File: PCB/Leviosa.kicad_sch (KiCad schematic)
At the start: 74 parts, among them J1 Barrel_Jack, J2 Conn_01x05_Socket, J3 2.54mm 1x03 Spare, Q1 NCE0110K, U1 STM32G030F6Px, U10 LM321, U2 TPS1H200AQDGNRQ1, U3 INA199A1DCKR, U4 L78L10_SOT89, U5 AZ1117CH2-3.3, U6 SS495A, U8 LM393, U9 MX27517

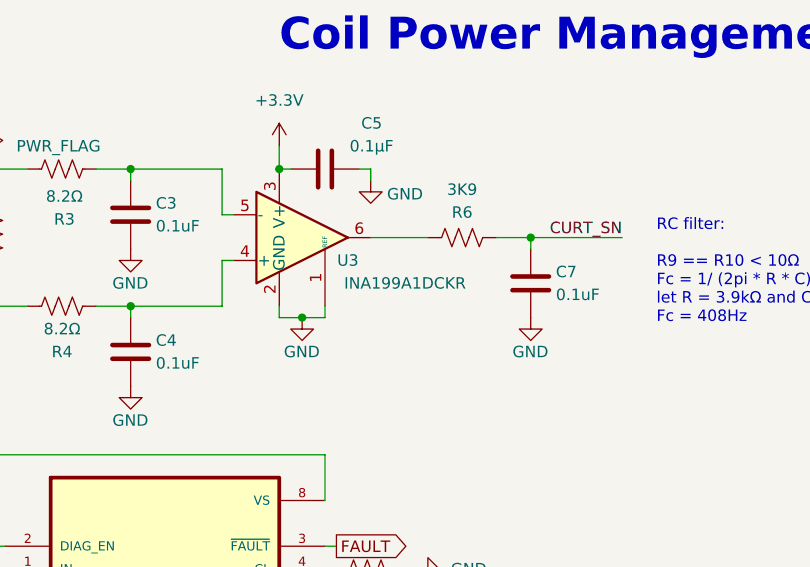
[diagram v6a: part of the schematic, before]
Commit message: Update current sense to 200V/V from 50V/V
Also updated footprint to hand solder version
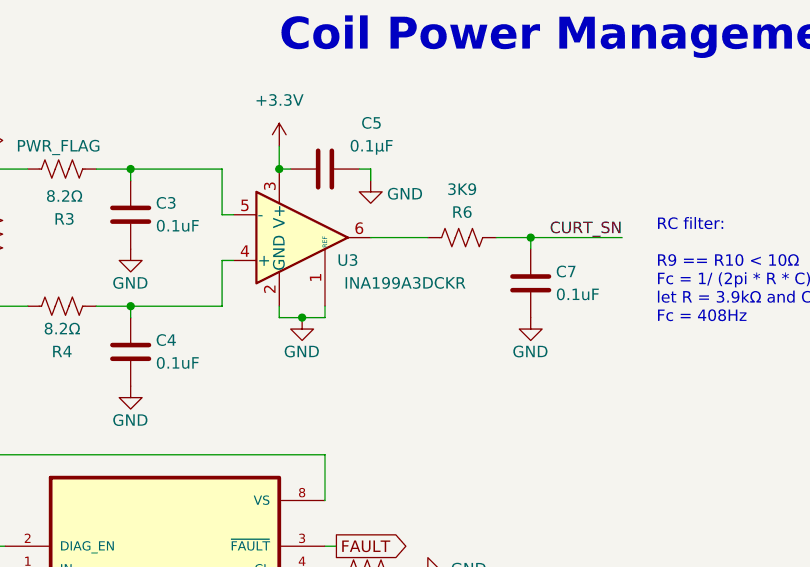
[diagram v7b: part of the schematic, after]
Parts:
- U3: value INA199A1DCKR -> INA199A3DCKR; footprint Package_TO_SOT_SMD:SOT-363_SC-70-6 -> Package_TO_SOT_SMD:SOT-363_SC-70-6_Handsoldering; Supplier https://www.lcsc.com/product-detail/C59135.html?s_z=n_INA199 -> https://www.lcsc.com/product-detail/C132098.html?s_z=n_INA1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
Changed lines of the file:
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@@
 			)
 		)
-		(property "Value" "INA199A1DCKR"
+		(property "Value" "INA199A3DCKR"
 			(at 100.33 49.53 0)
 			(effects
@@
 			)
 		)
-		(property "Footprint" "Package_TO_SOT_SMD:SOT-363_SC-70-6"
+		(property "Footprint" "Package_TO_SOT_SMD:SOT-363_SC-70-6_Handsoldering"
 			(at 90.17 43.18 0)
 			(effects
@@
 			)
 		)
-		(property "Supplier" "https://www.lcsc.com/product-detail/C59135.html?s_z=n_INA199"
+		(property "Supplier" "https://www.lcsc.com/product-detail/C132098.html?s_z=n_INA199&spm=wm.ssy.bg.3.xh&lcsc_vid=FgBdVFcAFQddBlFSEgVbXlBXRVlWBlZWRABaUgJXFgAxVlNRQ1RWVVVRQ1leVzsOAxUeFF5JWBYZEEoKFBINSQcJGk4dAgUUFAk%3D"
 			(at 88.9 44.45 0)
 			(effects

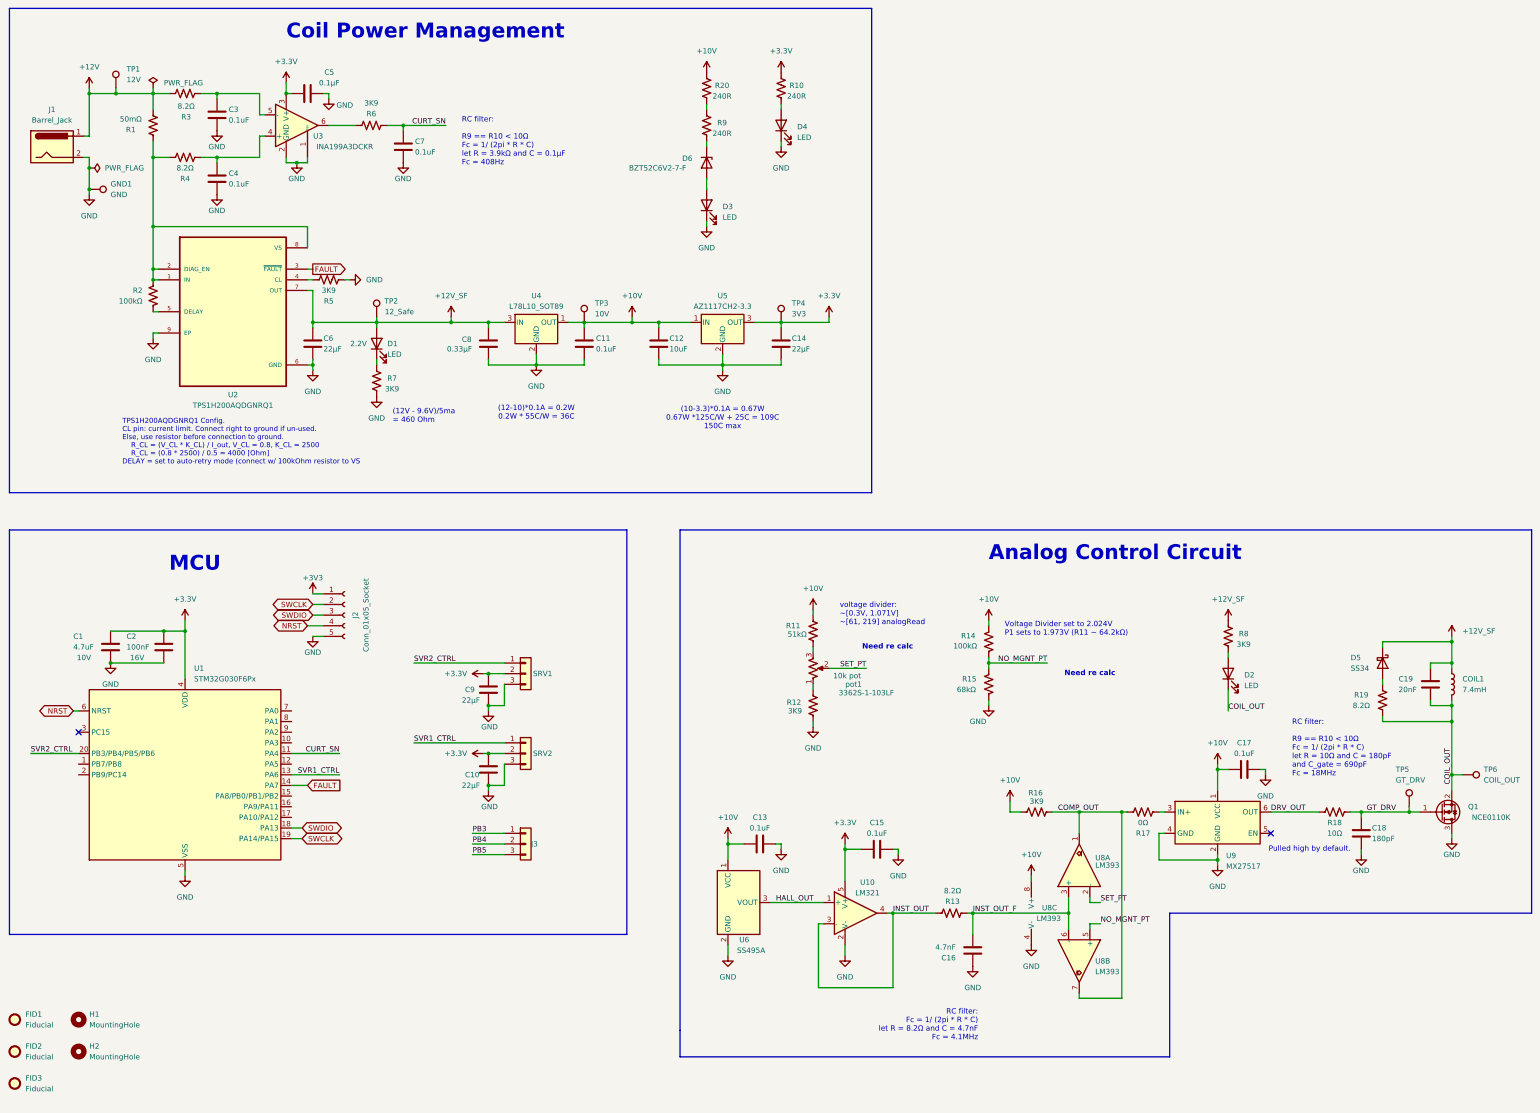
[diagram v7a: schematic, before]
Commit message: Changed LM321 to 10V
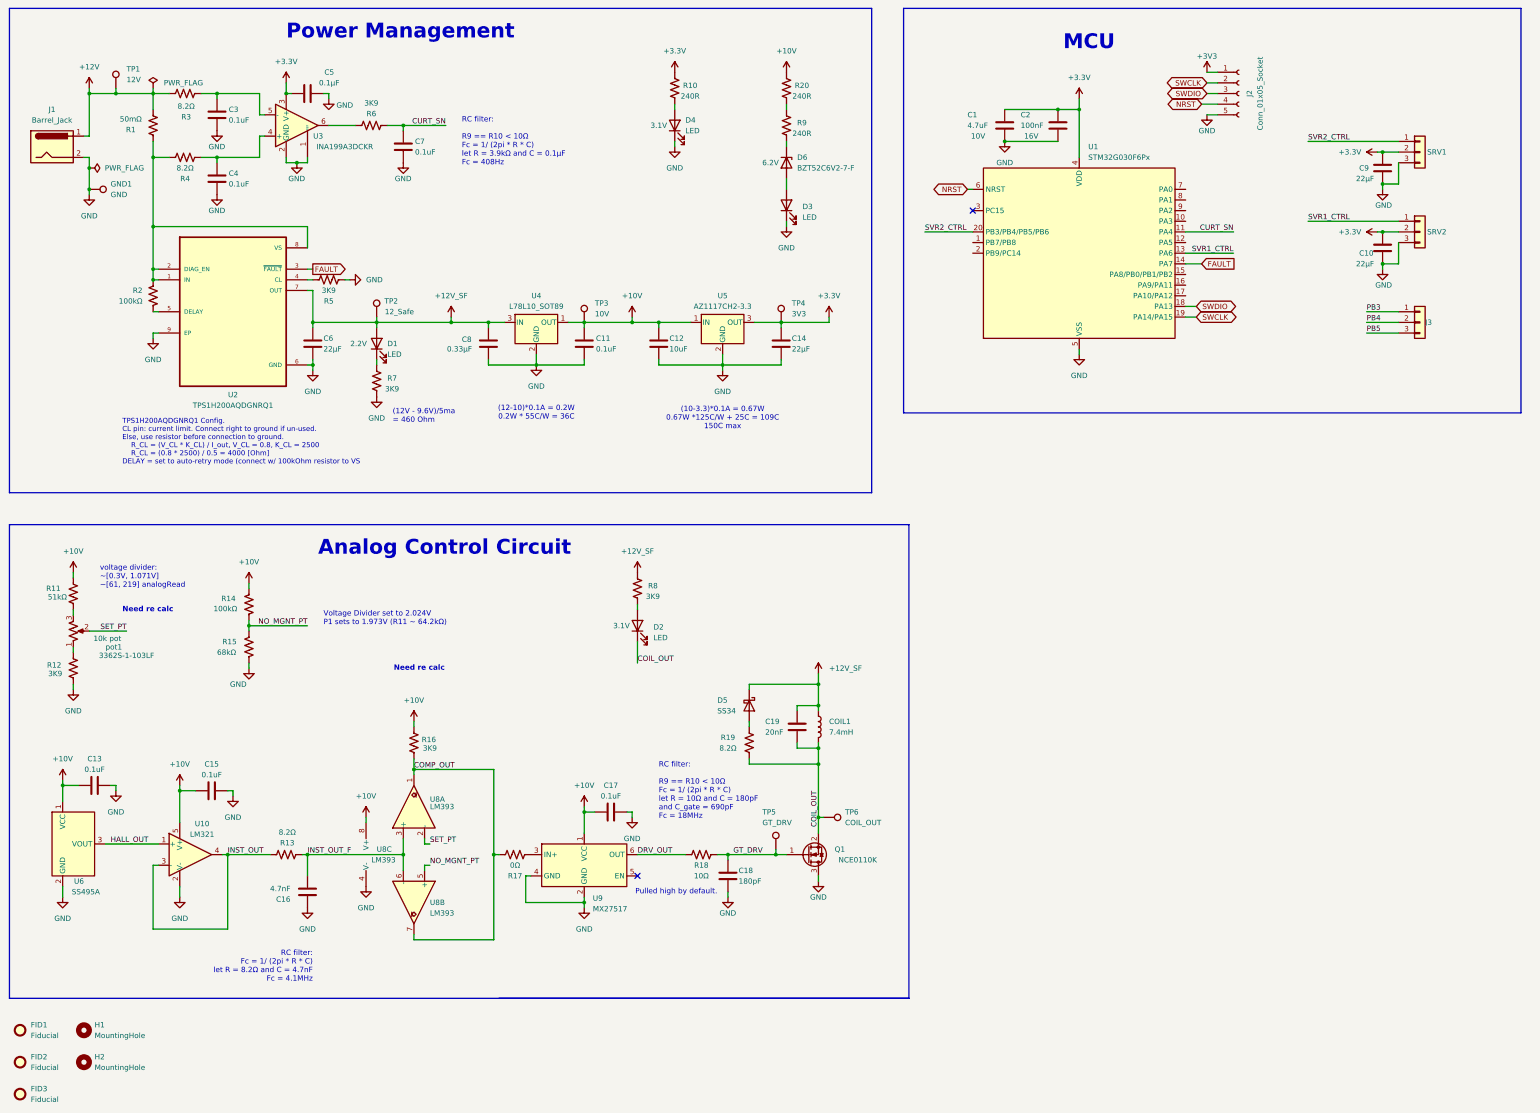
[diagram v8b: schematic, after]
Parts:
- D6: Vf (none) -> 6.2V
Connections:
- net +10V: now also C15.1, U10.5 (V+)
- net +3.3V: no longer C15.1, U10.5 (V+)
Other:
- note added: "Power Management"
- note removed: "Coil Power Management"
- moved on the sheet: C1, C10, C13, C15, C16, C17, C18, C19, C2, C9, COIL1, D2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
